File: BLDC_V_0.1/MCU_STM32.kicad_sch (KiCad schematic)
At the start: 30 parts, among them J2 SWD, J3 Conn_01x03, J4 Conn_01x04, J5 USB_B_Micro, U3 AMS1117, U3 USBLC6-2SC6, U5 STM32G473VET6, Y1 16MHz

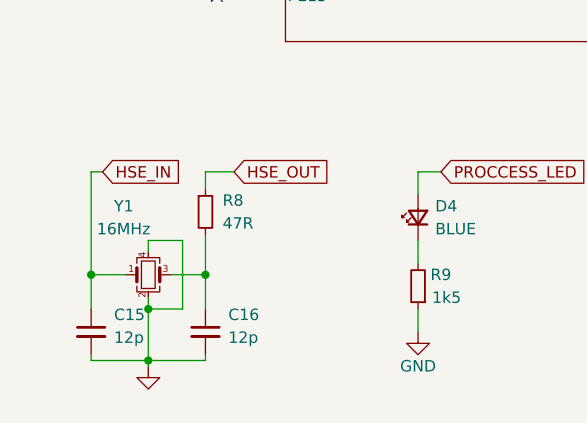
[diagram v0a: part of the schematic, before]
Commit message: Xtal changed 16MHz to 24MHz.
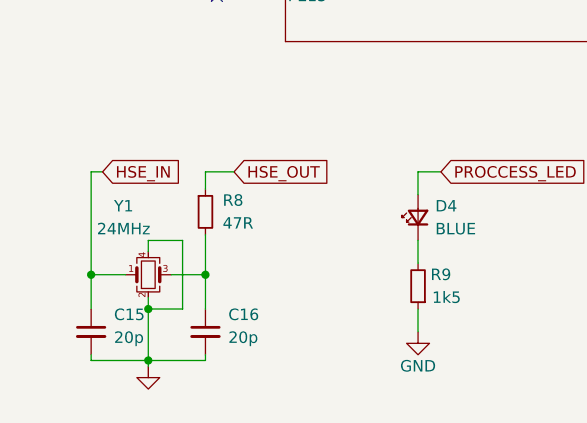
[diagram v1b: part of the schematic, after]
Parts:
- C15, C16: value 12p -> 20p
- Y1: value 16MHz -> 24MHz
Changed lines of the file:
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@@
       (effects (font (size 1.27 1.27)) (justify left))
     )
-    (property "Value" "12p" (at 34.29 190.373 0)
+    (property "Value" "20p" (at 34.29 190.373 0)
       (effects (font (size 1.27 1.27)) (justify left))
     )
@@
       (effects (font (size 1.27 1.27)) (justify left))
     )
-    (property "Value" "16MHz" (at 19.685 178.308 0)
+    (property "Value" "24MHz" (at 19.685 178.308 0)
       (effects (font (size 1.27 1.27)) (justify left))
     )
@@
       (effects (font (size 1.27 1.27)) (justify left))
     )
-    (property "Value" "12p" (at 21.59 190.373 0)
-      (effects (font (size 1.27 1.27)) (justify left))
-    )
+    (property "Value" "20p" (at 21.59 190.373 0)
+      (effects (font (size 1.27 1.27)) (justify left))
+    )

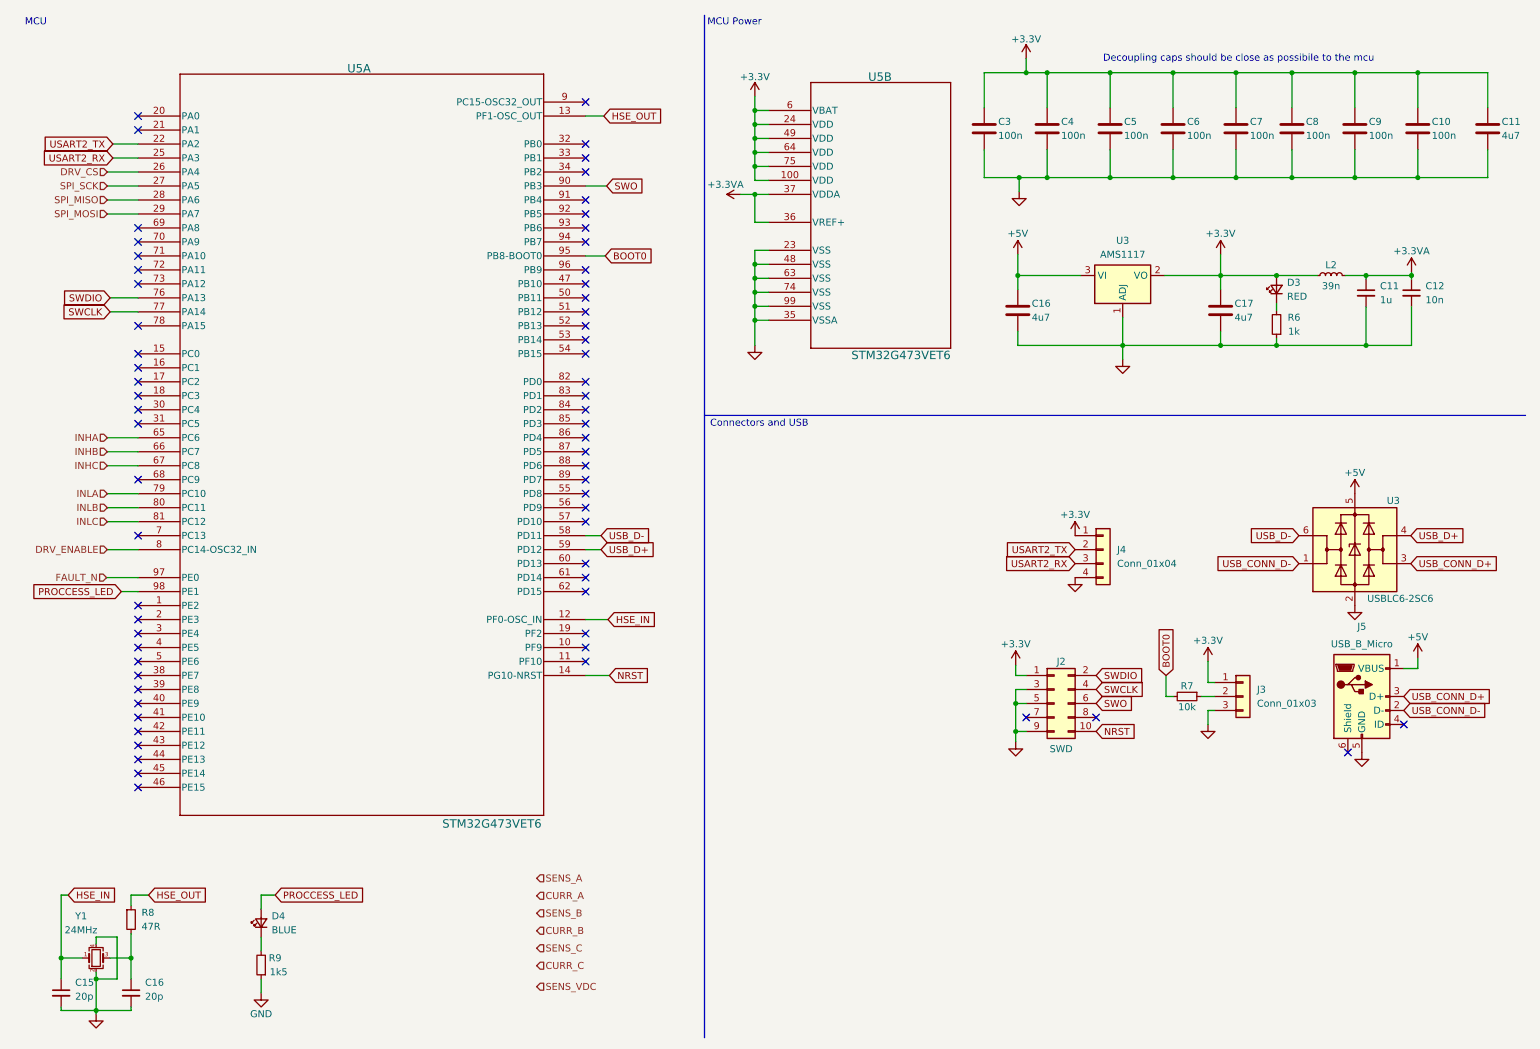
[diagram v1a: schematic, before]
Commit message: MCU VDD-VDDA-VREF pins checked and components added.
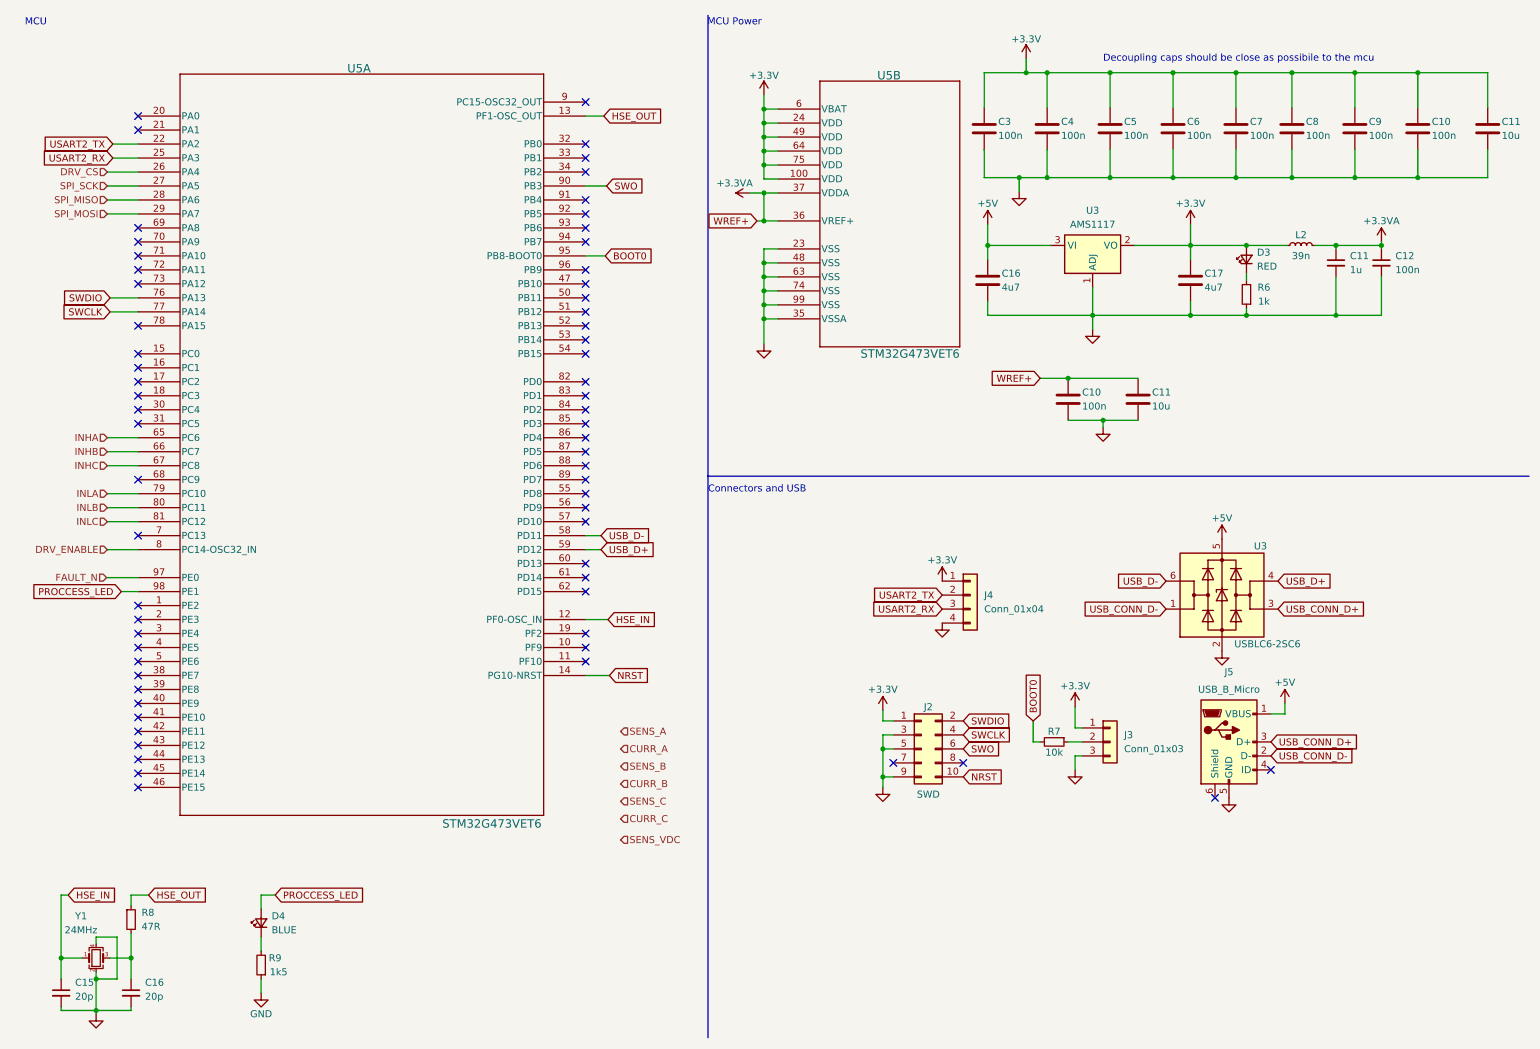
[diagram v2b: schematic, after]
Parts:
- added C10: 100n, symbol Device:C
- added C11: 10u, symbol Device:C
- C11: value 4u7 -> 10u
- C12: value 10n -> 100n
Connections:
- net +3.3VA: now also C10.1, C11.1
- net GND: now also C10.2, C11.2
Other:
- moved on the sheet: C11, C12, C16, C17, D3, J2, J3, J4, J5, L2, R6, R7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
